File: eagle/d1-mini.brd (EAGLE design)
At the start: 25.6 x 28.3 mm, 4 parts

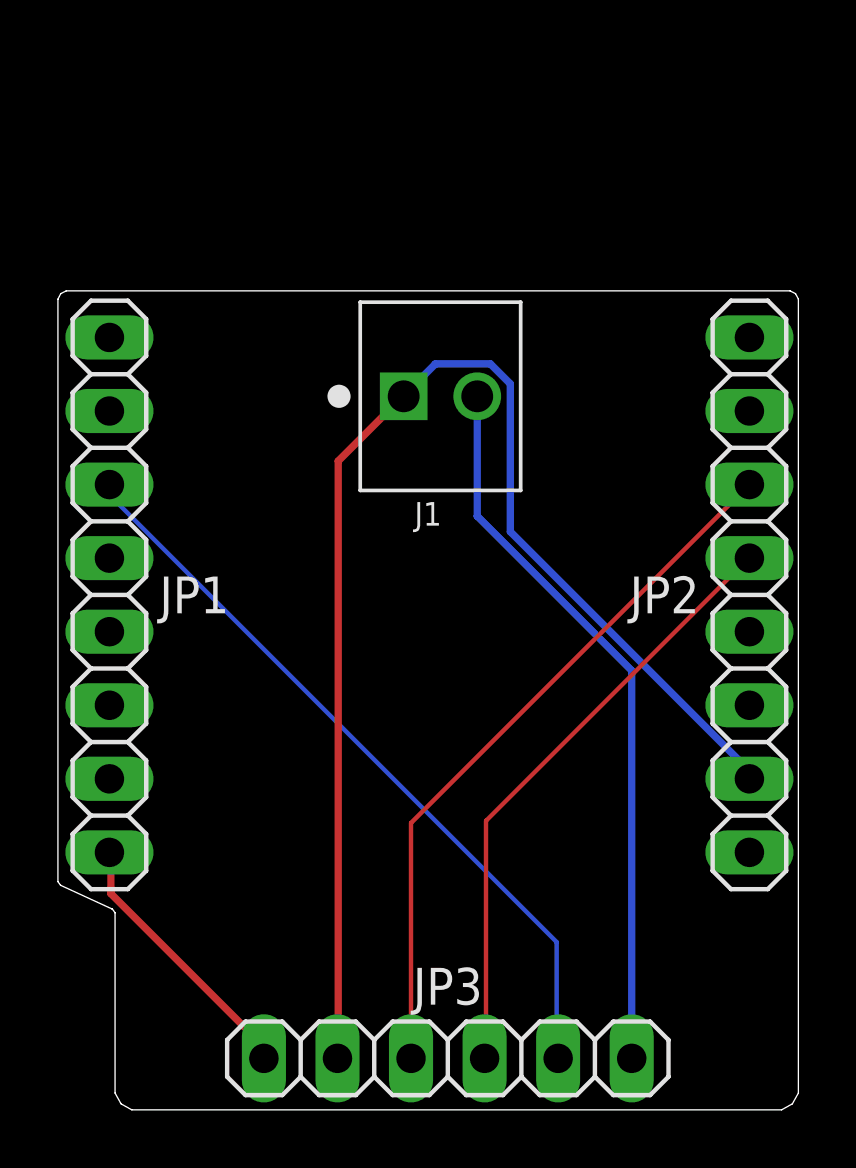
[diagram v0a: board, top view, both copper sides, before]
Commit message: switch d1-mini eagle board to use 2.54mm pin header for vbus/gnd and add text/oshw logo
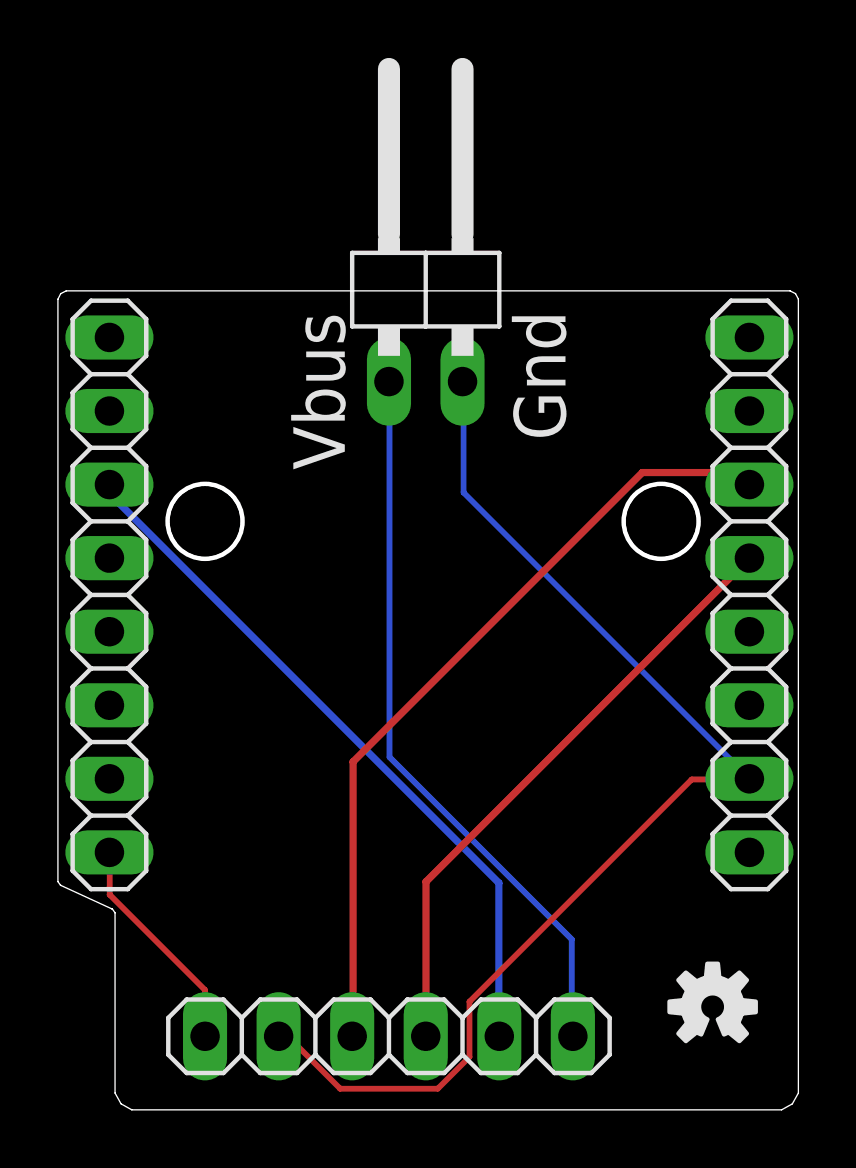
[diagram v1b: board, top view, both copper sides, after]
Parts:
- removed J1: (no value), 282834-2:CONN_282834-2
- added JP4: (no value), pinhead:1X02/90
- added LOGO1: OSHW-LOGOS, SparkFun-Aesthetics:OSHW-LOGO-S
- moved JP3 2.17 mm to (11.4, 2.54)
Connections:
- net GND: now also JP4.2; no longer J1.1
- net VBUS: now also JP4.1; no longer J1.2
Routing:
- net GND: track 45.3 -> 40.4 mm
- net SCL: track 24.7 -> 27.5 mm
- net ALERT: track 26.2 -> 24.6 mm
- net 3V3: track 9.32 -> 7.71 mm
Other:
- outline, holes or cut-outs redrawn
- board text added: "Gnd"
- board text added: "PowerProf r1"
- board text added: "Vbus"
- board text added: "https://github.com/powerprof"

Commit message: update and sync all schematics and images - fix labels and add consistent attribution
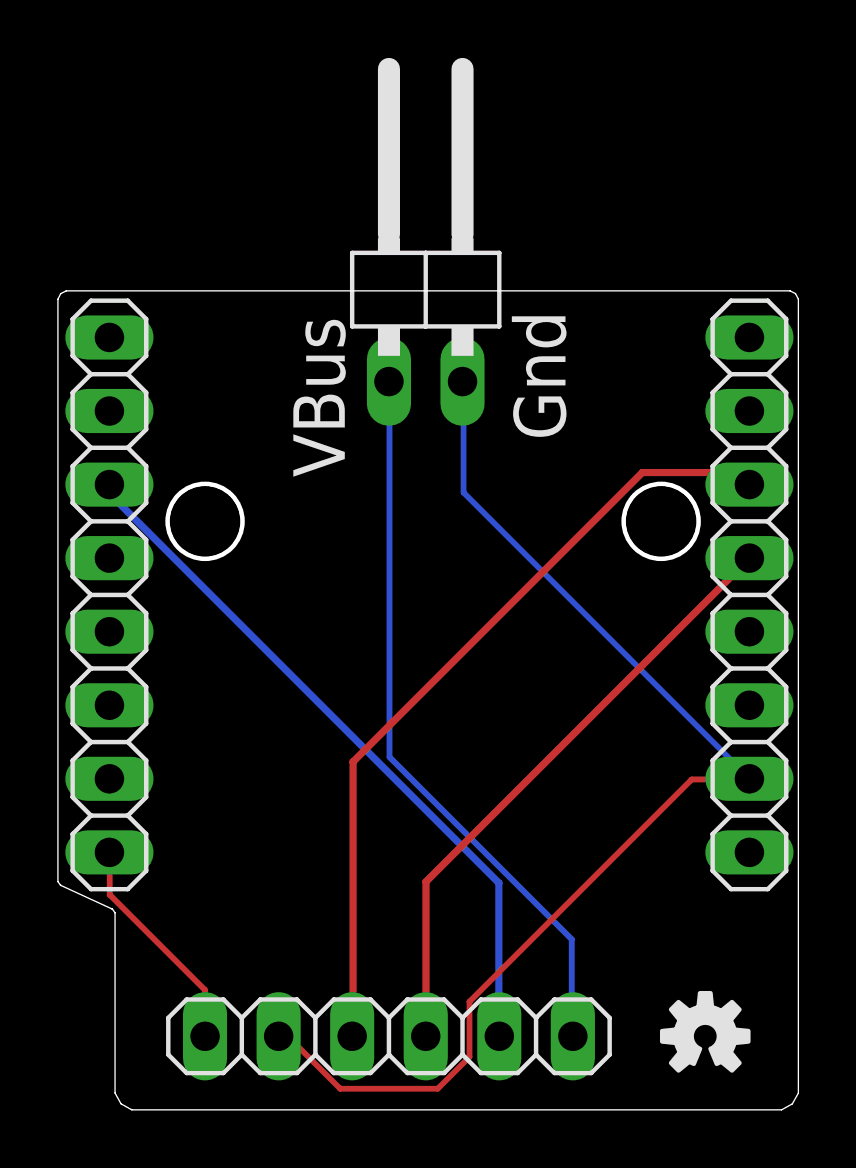
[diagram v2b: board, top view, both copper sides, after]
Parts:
- moved LOGO1 1.05 mm to (22.4, 2.54)
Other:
- board text added: "MIT License - by ayan4m1"
- board text added: "VBus"
- board text removed: "Vbus"
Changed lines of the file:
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@@
 <setting verticaltext="up"/>
 </settings>
-<grid distance="10" unitdist="mil" unit="mil" style="lines" multiple="1" display="yes" altdistance="5" altunitdist="mil" altunit="mil"/>
+<grid distance="10" unitdist="mil" unit="mil" style="lines" multiple="1" display="no" altdistance="5" altunitdist="mil" altunit="mil"/>
 <layers>
 <layer number="1" name="Top" color="4" fill="1" visible="yes" active="yes"/>
@@
 <layer number="14" name="Route14" color="22" fill="1" visible="no" active="no"/>
 <layer number="15" name="Route15" color="23" fill="1" visible="no" active="no"/>
-<layer number="16" name="Bottom" color="1" fill="1" visible="yes" active="yes"/>
+<layer number="16" name="Bottom" color="1" fill="1" visible="no" active="yes"/>
 <layer number="17" name="Pads" color="2" fill="1" visible="yes" active="yes"/>
 <layer number="18" name="Vias" color="2" fill="1" visible="yes" active="yes"/>
@@
 <layer number="20" name="Dimension" color="24" fill="1" visible="yes" active="yes"/>
 <layer number="21" name="tPlace" color="7" fill="1" visible="yes" active="yes"/>
-<layer number="22" name="bPlace" color="7" fill="1" visible="yes" active="yes"/>
+<layer number="22" name="bPlace" color="7" fill="1" visible="no" active="yes"/>
 <layer number="23" name="tOrigins" color="15" fill="1" visible="yes" active="yes"/>
-<layer number="24" name="bOrigins" color="15" fill="1" visible="yes" active="yes"/>
+<layer number="24" name="bOrigins" color="15" fill="1" visible="no" active="yes"/>
 <layer number="25" name="tNames" color="7" fill="1" visible="yes" active="yes"/>
-<layer number="26" name="bNames" color="7" fill="1" visible="yes" active="yes"/>
+<layer number="26" name="bNames" color="7" fill="1" visible="no" active="yes"/>
 <layer number="27" name="tValues" color="7" fill="1" visible="no" active="yes"/>
 <layer number="28" name="bValues" color="7" fill="1" visible="no" active="yes"/>
@@
 <layer number="38" name="bTest" color="7" fill="1" visible="no" active="yes"/>
 <layer number="39" name="tKeepout" color="4" fill="11" visible="yes" active="yes"/>
-<layer number="40" name="bKeepout" color="1" fill="11" visible="yes" active="yes"/>
+<layer number="40" name="bKeepout" color="1" fill="11" visible="no" active="yes"/>
 <layer number="41" name="tRestrict" color="4" fill="10" visible="yes" active="yes"/>
-<layer number="42" name="bRestrict" color="1" fill="10" visible="yes" active="yes"/>
+<layer number="42" name="bRestrict" color="1" fill="10" visible="no" active="yes"/>
 <layer number="43" name="vRestrict" color="2" fill="10" visible="no" active="yes"/>
 <layer number="44" name="Drills" color="7" fill="1" visible="no" active="yes"/>
@@
 <layer number="50" name="dxf" color="7" fill="1" visible="no" active="no"/>
 <layer number="51" name="tDocu" color="7" fill="1" visible="yes" active="yes"/>
-<layer number="52" name="bDocu" color="7" fill="1" visible="yes" active="yes"/>
+<layer number="52" name="bDocu" color="7" fill="1" visible="no" active="yes"/>
 <layer number="53" name="tGND_GNDA" color="7" fill="9" visible="no" active="no"/>
 <layer number="54" name="bGND_GNDA" color="1" fill="9" visible="no" active="no"/>
@@
 <wire x1="25.4689" y1="28.1823" x2="25.2788" y2="28.2787" width="0.001" layer="20"/>
 <circle x="5.08" y="20.32" radius="1.29515" width="0.1524" layer="20"/>
-<text x="9.906" y="22.098" size="1.778" layer="25" rot="R90">Vbus</text>
 <text x="17.526" y="23.114" size="1.778" layer="25" rot="R90">Gnd</text>
 <circle x="20.828" y="20.32" radius="1.29515" width="0.1524" layer="20"/>
@@
 <text x="20.066" y="16.002" size="1.778" layer="22" rot="MR0">PowerProf r1</text>
 <text x="20.066" y="14.224" size="0.8128" layer="22" rot="MR0">https://github.com/powerprof</text>
+<text x="19.558" y="12.446" size="0.8128" layer="26" rot="MR0">MIT License - by ayan4m1</text>
+<text x="9.906" y="21.844" size="1.778" layer="25" rot="R90">VBus</text>
 </plain>
 <attributes>
@@
 <attribute name="VALUE" x="17.145" y="25.146" size="1.27" layer="27" rot="R90"/>
 </element>
-<element name="LOGO1" library="SparkFun-Aesthetics" package="OSHW-LOGO-S" value="OSHW-LOGOS" x="22.606" y="3.556" smashed="yes"/>
+<element name="LOGO1" library="SparkFun-Aesthetics" package="OSHW-LOGO-S" value="OSHW-LOGOS" x="22.352" y="2.54" smashed="yes"/>
 </elements>
 <signals>

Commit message: update clearances to 8mil (thanks tech-tx!)
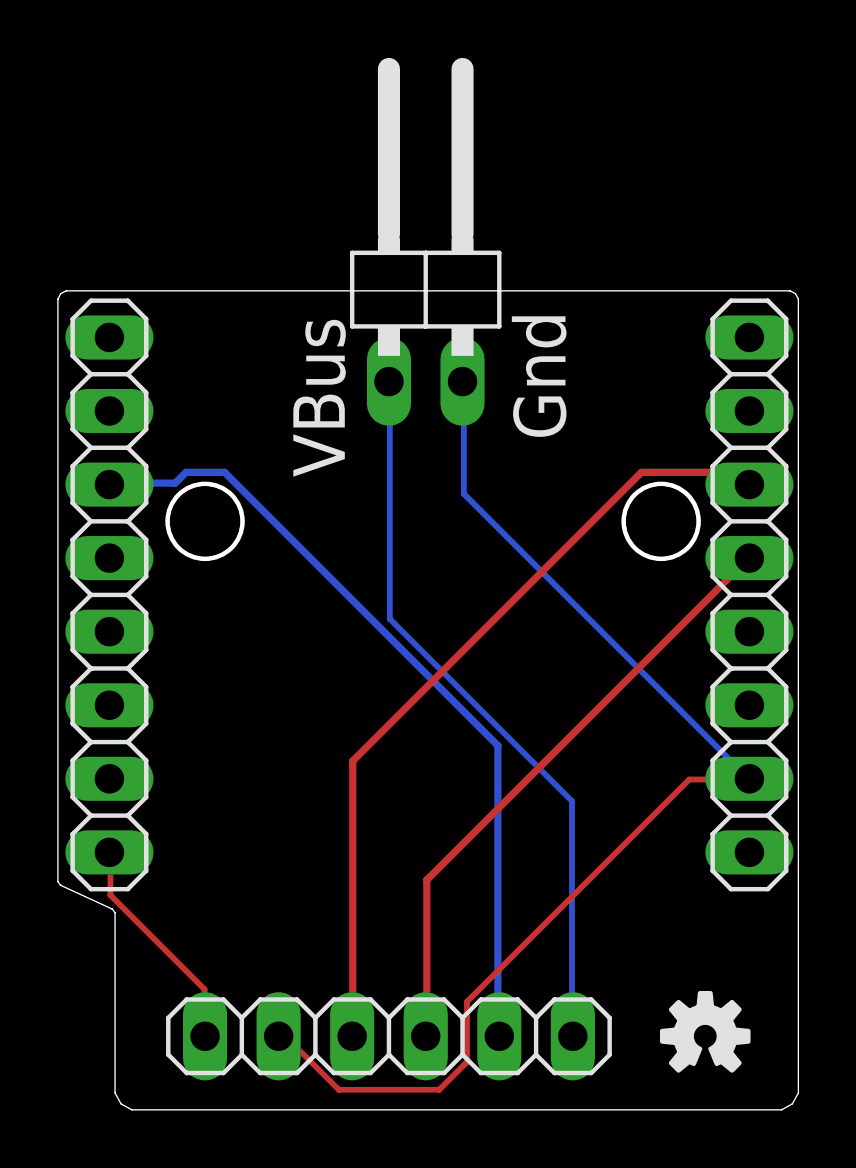
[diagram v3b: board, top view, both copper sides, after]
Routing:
- net ALERT: track 24.6 -> 27.6 mm

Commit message: sync boards to use same net classes, update images with new traces
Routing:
- net ALERT: track 27.6 -> 24.6 mm
- net GND: track 40.5 -> 43.1 mm
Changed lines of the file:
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@@
 </variantdefs>
 <classes>
-<class number="0" name="default" width="0" drill="0">
+<class number="0" name="default" width="0.1524" drill="0">
 </class>
-<class number="1" name="current" width="0.2" drill="0">
+<class number="1" name="current" width="0.635" drill="0">
 </class>
-<class number="2" name="signal" width="0.25" drill="0">
+<class number="2" name="signal" width="0.2032" drill="0">
 </class>
 </classes>
@@
 <contactref element="JP1" pad="1"/>
 <contactref element="JP3" pad="1"/>
-<wire x1="1.8122" y1="7.4087" x2="1.8122" y2="8.8478" width="0.2" layer="1"/>
-<wire x1="5.0635" y1="4.1574" x2="1.8122" y2="7.4087" width="0.2" layer="1"/>
-<wire x1="5.0635" y1="2.5584" x2="5.0635" y2="4.1574" width="0.2" layer="1"/>
-<wire x1="1.8122" y1="8.8478" x2="1.778" y2="8.89" width="0.2" layer="1"/>
-<wire x1="5.0635" y1="2.5584" x2="5.08" y2="2.54" width="0.2" layer="1"/>
+<wire x1="1.778" y1="7.8232" x2="1.778" y2="8.89" width="0.635" layer="1"/>
+<wire x1="5.0673" y1="4.5339" x2="1.778" y2="7.8232" width="0.635" layer="1"/>
+<wire x1="5.0673" y1="2.5781" x2="5.0673" y2="4.5339" width="0.635" layer="1"/>
+<wire x1="5.0673" y1="2.5781" x2="5.08" y2="2.54" width="0.635" layer="1"/>
 </signal>
 <signal name="SCL" class="2">
 <contactref element="JP2" pad="3"/>
 <contactref element="JP3" pad="3"/>
-<wire x1="10.1803" y1="12.0458" x2="10.1803" y2="2.5584" width="0.25" layer="1"/>
-<wire x1="20.1474" y1="22.0129" x2="10.1803" y2="12.0458" width="0.25" layer="1"/>
-<wire x1="23.452" y1="22.0129" x2="20.1474" y2="22.0129" width="0.25" layer="1"/>
-<wire x1="23.8251" y1="21.6398" x2="23.452" y2="22.0129" width="0.25" layer="1"/>
-<wire x1="10.1803" y1="2.5584" x2="10.16" y2="2.54" width="0.25" layer="1"/>
-<wire x1="23.8251" y1="21.6398" x2="23.876" y2="21.59" width="0.25" layer="1"/>
+<wire x1="10.2235" y1="12.0904" x2="10.2235" y2="2.5781" width="0.2032" layer="1"/>
+<wire x1="20.0914" y1="21.9583" x2="10.2235" y2="12.0904" width="0.2032" layer="1"/>
+<wire x1="23.4696" y1="21.9583" x2="20.0914" y2="21.9583" width="0.2032" layer="1"/>
+<wire x1="23.8252" y1="21.6027" x2="23.4696" y2="21.9583" width="0.2032" layer="1"/>
+<wire x1="10.2235" y1="2.5781" x2="10.16" y2="2.54" width="0.2032" layer="1"/>
+<wire x1="23.8252" y1="21.6027" x2="23.876" y2="21.59" width="0.2032" layer="1"/>
 </signal>
 <signal name="SDA" class="2">
 <contactref element="JP2" pad="4"/>
 <contactref element="JP3" pad="4"/>
-<wire x1="12.7387" y1="7.9417" x2="12.7387" y2="2.5584" width="0.25" layer="1"/>
-<wire x1="23.8251" y1="19.0281" x2="12.7387" y2="7.9417" width="0.25" layer="1"/>
-<wire x1="12.7387" y1="2.5584" x2="12.7" y2="2.54" width="0.25" layer="1"/>
-<wire x1="23.8251" y1="19.0281" x2="23.876" y2="19.05" width="0.25" layer="1"/>
+<wire x1="12.7127" y1="7.9121" x2="12.7127" y2="2.5781" width="0.2032" layer="1"/>
+<wire x1="23.8252" y1="19.0246" x2="12.7127" y2="7.9121" width="0.2032" layer="1"/>
+<wire x1="12.7127" y1="2.5781" x2="12.7" y2="2.54" width="0.2032" layer="1"/>
+<wire x1="23.8252" y1="19.0246" x2="23.876" y2="19.05" width="0.2032" layer="1"/>
 </signal>
 <signal name="GND" class="1">
@@
 <contactref element="JP3" pad="2"/>
 <contactref element="JP4" pad="2"/>
-<wire x1="7.8884" y1="2.5051" x2="7.6219" y2="2.5051" width="0.2" layer="1"/>
-<wire x1="9.7006" y1="0.6929" x2="7.8884" y2="2.5051" width="0.2" layer="1"/>
-<wire x1="13.1651" y1="0.6929" x2="9.7006" y2="0.6929" width="0.2" layer="1"/>
-<wire x1="14.1245" y1="1.6523" x2="13.1651" y2="0.6929" width="0.2" layer="1"/>
-<wire x1="14.1245" y1="3.731" x2="14.1245" y2="1.6523" width="0.2" layer="1"/>
-<wire x1="21.7997" y1="11.4062" x2="14.1245" y2="3.731" width="0.2" layer="1"/>
-<wire x1="23.8251" y1="11.4062" x2="21.7997" y2="11.4062" width="0.2" layer="1"/>
-<wire x1="7.6219" y1="2.5051" x2="7.62" y2="2.54" width="0.2" layer="1"/>
-<wire x1="23.8251" y1="11.4062" x2="23.876" y2="11.43" width="0.2" layer="1"/>
-<wire x1="14.0179" y1="21.2667" x2="14.0179" y2="25.1043" width="0.2" layer="16"/>
-<wire x1="23.8251" y1="11.4595" x2="14.0179" y2="21.2667" width="0.2" layer="16"/>
-<wire x1="14.0179" y1="25.1043" x2="13.97" y2="25.146" width="0.2" layer="16"/>
-<wire x1="23.8251" y1="11.4595" x2="23.876" y2="11.43" width="0.2" layer="16"/>
+<wire x1="7.6454" y1="18.7579" x2="7.6454" y2="2.5781" width="0.635" layer="1"/>
+<wire x1="13.9573" y1="25.0698" x2="7.6454" y2="18.7579" width="0.635" layer="1"/>
+<wire x1="7.6454" y1="2.5781" x2="7.62" y2="2.54" width="0.635" layer="1"/>
+<wire x1="13.9573" y1="25.0698" x2="13.97" y2="25.146" width="0.635" layer="1"/>
+<wire x1="22.6695" y1="12.6238" x2="23.8252" y2="11.4681" width="0.635" layer="16"/>
+<wire x1="22.5806" y1="12.6238" x2="22.6695" y2="12.6238" width="0.635" layer="16"/>
+<wire x1="14.0462" y1="21.1582" x2="22.5806" y2="12.6238" width="0.635" layer="16"/>
+<wire x1="14.0462" y1="25.0698" x2="14.0462" y2="21.1582" width="0.635" layer="16"/>
+<wire x1="23.8252" y1="11.4681" x2="23.876" y2="11.43" width="0.635" layer="16"/>
+<wire x1="14.0462" y1="25.0698" x2="13.97" y2="25.146" width="0.635" layer="16"/>
 </signal>
 <signal name="ALERT" class="2">
 <contactref element="JP3" pad="5"/>
 <contactref element="JP1" pad="6"/>
-<wire x1="4.0508" y1="21.6398" x2="1.8122" y2="21.6398" width="0.25" layer="16"/>
-<wire x1="4.4239" y1="22.0129" x2="4.0508" y2="21.6398" width="0.25" layer="16"/>
-<wire x1="5.7564" y1="22.0129" x2="4.4239" y2="22.0129" width="0.25" layer="16"/>
-<wire x1="15.1905" y1="12.5788" x2="5.7564" y2="22.0129" width="0.25" layer="16"/>
-<wire x1="15.1905" y1="2.5584" x2="15.1905" y2="12.5788" width="0.25" layer="16"/>
-<wire x1="1.8122" y1="21.6398" x2="1.778" y2="21.59" width="0.25" layer="16"/>
-<wire x1="15.1905" y1="2.5584" x2="15.24" y2="2.54" width="0.25" layer="16"/>
+<wire x1="1.778" y1="21.336" x2="1.778" y2="21.59" width="0.2032" layer="16"/>
+<wire x1="3.6449" y1="19.4691" x2="1.778" y2="21.336" width="0.2032" layer="16"/>
+<wire x1="3.6449" y1="14.1351" x2="3.6449" y2="19.4691" width="0.2032" layer="16"/>
+<wire x1="15.24" y1="2.54" x2="3.6449" y2="14.1351" width="0.2032" layer="16"/>
 </signal>
 <signal name="VBUS" class="1">
 <contactref element="JP3" pad="6"/>
 <contactref element="JP4" pad="1"/>
-<wire x1="11.4595" y1="16.9494" x2="11.4595" y2="25.1043" width="0.2" layer="16"/>
-<wire x1="17.7489" y1="10.66" x2="11.4595" y2="16.9494" width="0.2" layer="16"/>
-<wire x1="17.7489" y1="2.5584" x2="17.7489" y2="10.66" width="0.2" layer="16"/>
-<wire x1="11.4595" y1="25.1043" x2="11.43" y2="25.146" width="0.2" layer="16"/>
-<wire x1="17.7489" y1="2.5584" x2="17.78" y2="2.54" width="0.2" layer="16"/>
+<wire x1="11.4681" y1="8.89" x2="11.4681" y2="25.0698" width="0.635" layer="16"/>
+<wire x1="17.78" y1="2.5781" x2="11.4681" y2="8.89" width="0.635" layer="16"/>
+<wire x1="11.4681" y1="25.0698" x2="11.43" y2="25.146" width="0.635" layer="16"/>
+<wire x1="17.78" y1="2.5781" x2="17.78" y2="2.54" width="0.635" layer="16"/>
 </signal>
 </signals>
